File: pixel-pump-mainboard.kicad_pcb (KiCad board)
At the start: 4 copper layers, 68 x 67.3 mm, 123 parts, among them J1 JST NC Valve, J10 BM10B-SRSS-TB(LF)(SN), J11 UART/SWD DNP, J12 TYPE-C-31-M-12, J2 JST NO Valve, J3 6P4C, J4 JST 3 Way Valve, J5 Jack-DC, J6 Phoenix Contact 1733570, J7 BM04B-SRSS-TBT(LF)(SN), J8 SPI, J9 BM04B-SRSS-TBT(LF)(SN), Q1 BSS138, Q2 BSS138, Q3 BSS138, Q4 STN4NF20L, Q5 BSS138, SW1 BOOTSEL, U1 LD1117S33TR, U2 TPS62112RSAR, U3 W25Q128JVPIQ TR, U4 RP2040, Y1 ABMM2-12.000MHZ-E2-T

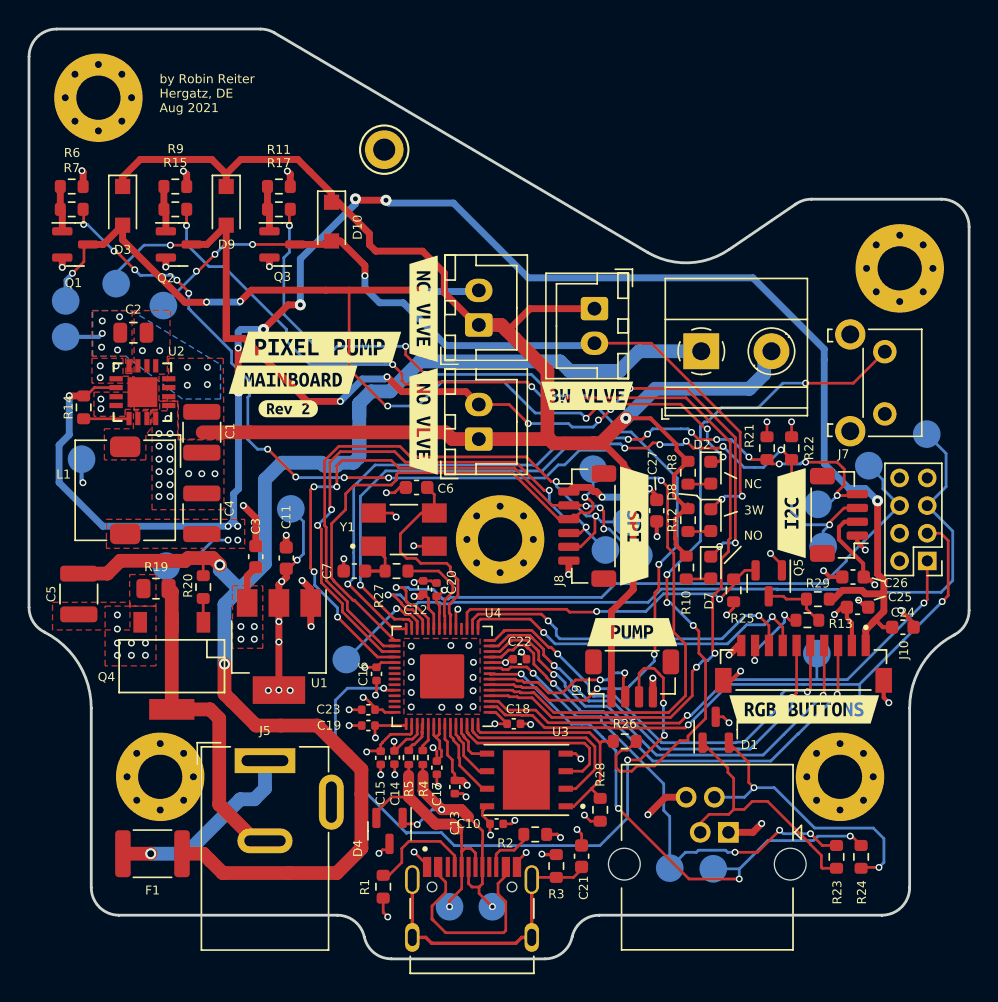
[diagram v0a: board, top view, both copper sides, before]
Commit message: Rename entire project to pixel pump
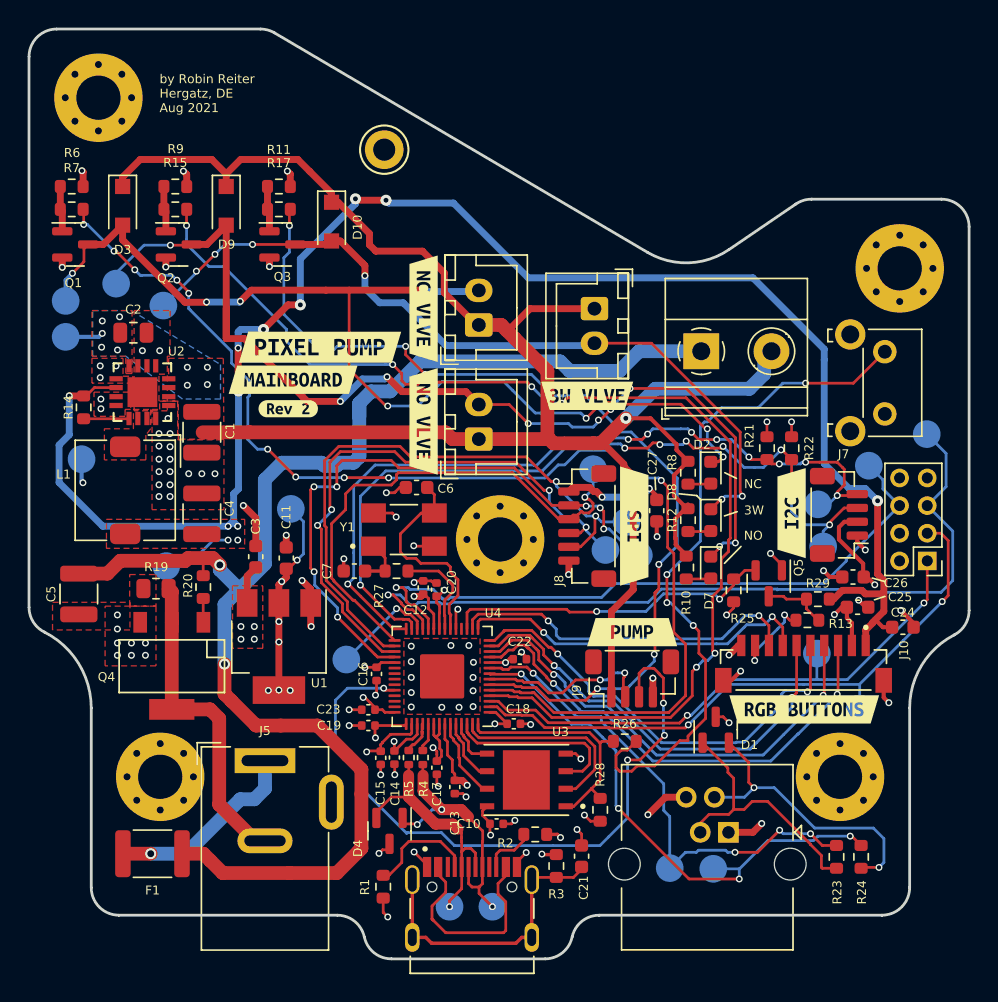
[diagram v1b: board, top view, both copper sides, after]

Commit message: Updated layout for EMI specific changes
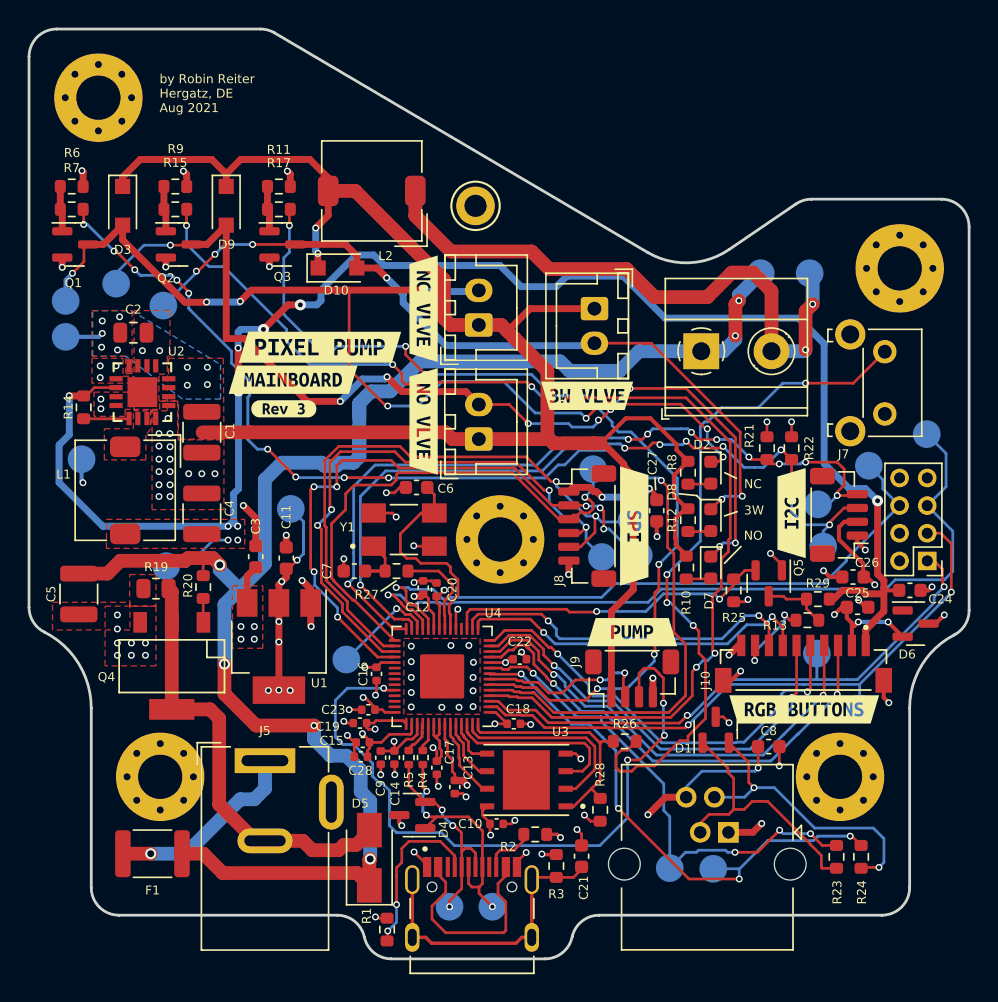
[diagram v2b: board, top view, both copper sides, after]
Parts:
- removed kibuzzard-61080B37: G***, kibuzzard-61080B37
- added C28: DNP, Capacitor_SMD:C_0402_1005Metric, F.Cu at (90.0, 143.0)
- added C8: 100n, Capacitor_SMD:C_0603_1608Metric, F.Cu at (119.5, 142.2)
- added C9: DNP, Capacitor_SMD:C_0402_1005Metric, F.Cu at (91.4, 143.0)
- added D5: SMAJ12CA, Diode_SMD:D_SMA, F.Cu at (90.6, 150.3)
- added D6: SP0502BAHT, Package_TO_SOT_SMD:SOT-23, F.Cu at (130.1, 133.3)
- added L2: 6.8uH, Inductor_SMD:L_TDK_SLF7032, F.Cu at (90.8, 102.0)
- added TP3: PSW1, TestPoint:TestPoint_Pad_D2.0mm, B.Cu at (118.9, 108.0)
- added TP6: PSW2, TestPoint:TestPoint_Pad_D2.0mm, B.Cu at (122.5, 108.0)
- added kibuzzard-61DF0B83: G***, kibuzzard-61DF0B83, F.Cu at (84.4, 117.8)
- C14, C15: value 1u -> 2.2u
- D2, D7, D8: value LED -> LED DNP
- J5: value Jack-DC -> Jack-DC 12V
- J6: value Phoenix Contact 1733570 -> Power Sw
- J7: value BM04B-SRSS-TBT(LF)(SN) -> I2C
- R10, R12, R8: value 68k -> 68k DNP
- R15, R17, R7: value 160 -> 220
- U3: value W25Q128JVPIQ TR -> W25Q128JVS
- moved TP19 7.75 mm to (98.3, 103.1)
- moved D10 3.38 mm to (88.3, 107.6), turned to 0 degrees
- moved R1 3.11 mm to (91.9, 155.5), turned to -90 degrees
- moved C24 2.71 mm to (129.7, 130.9)
- moved D4 2.01 mm to (93.7, 147.2), turned to 180 degrees
- moved C15 1.71 mm to (90.1, 141.9), turned to 180 degrees
- moved C19 0.64 mm to (89.9, 140.5)
- moved TP27 0.57 mm to (107.4, 128.5)
- moved TP28 0.40 mm to (109.6, 125.9)
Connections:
- J6 pad 2: +12V -> Net-(J6-Pad2)
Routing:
- net Net-(J6-Pad2): track 0.00 -> 44.0 mm, vias 0 -> 2
- net +3V3: track 71.9 -> 85.6 mm, vias 26 -> 29
- net Net-(C5-Pad1): track 105.2 -> 117.2 mm, vias 2 -> 6
- net Net-(D5-Pad2): track 23.2 -> 31.7 mm
- net +12V: track 137.2 -> 129.8 mm, vias 10 -> 11
- net +5V: track 130.0 -> 125.4 mm, vias 16 -> 14
- net Net-(J12-PadA5): track 8.27 -> 12.4 mm, vias 0 -> 2
- net DN: track 18.8 -> 14.9 mm, vias 1 -> 3
- net GND: track 59.7 -> 62.8 mm, vias 91 -> 94
- net UART0_RX: track 40.7 -> 42.4 mm
- net Net-(D7-Pad1): track 73.4 -> 72.0 mm
- net BEMF: track 49.4 -> 50.3 mm
- net DP: track 18.6 -> 17.8 mm
- net Drop Btn: track 34.6 -> 33.8 mm
- net +1V1: track 31.5 -> 32.3 mm
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
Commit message: Finish EMI changes
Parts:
- moved D5 0.37 mm to (90.5, 150.6), turned to -90 degrees
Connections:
- D5 pad 1: Net-(C5-Pad1) -> Net-(J5-Pad1)
- F1 pad 2: Net-(F1-Pad2) -> Net-(J5-Pad1)
- J5 pad 1: Net-(F1-Pad2) -> Net-(J5-Pad1)
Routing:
- net Net-(J5-Pad1): track 0.00 -> 37.6 mm, vias 0 -> 2
- net Net-(C5-Pad1): track 117.2 -> 95.2 mm
- net Net-(F1-Pad2): track 14.2 -> 0.00 mm, vias 1 -> 0
- net +1V1: track 32.3 -> 32.9 mm
- net Net-(D5-Pad2): track 31.7 -> 32.2 mm
- net BEMF: track 50.3 -> 50.7 mm, vias 4 -> 6

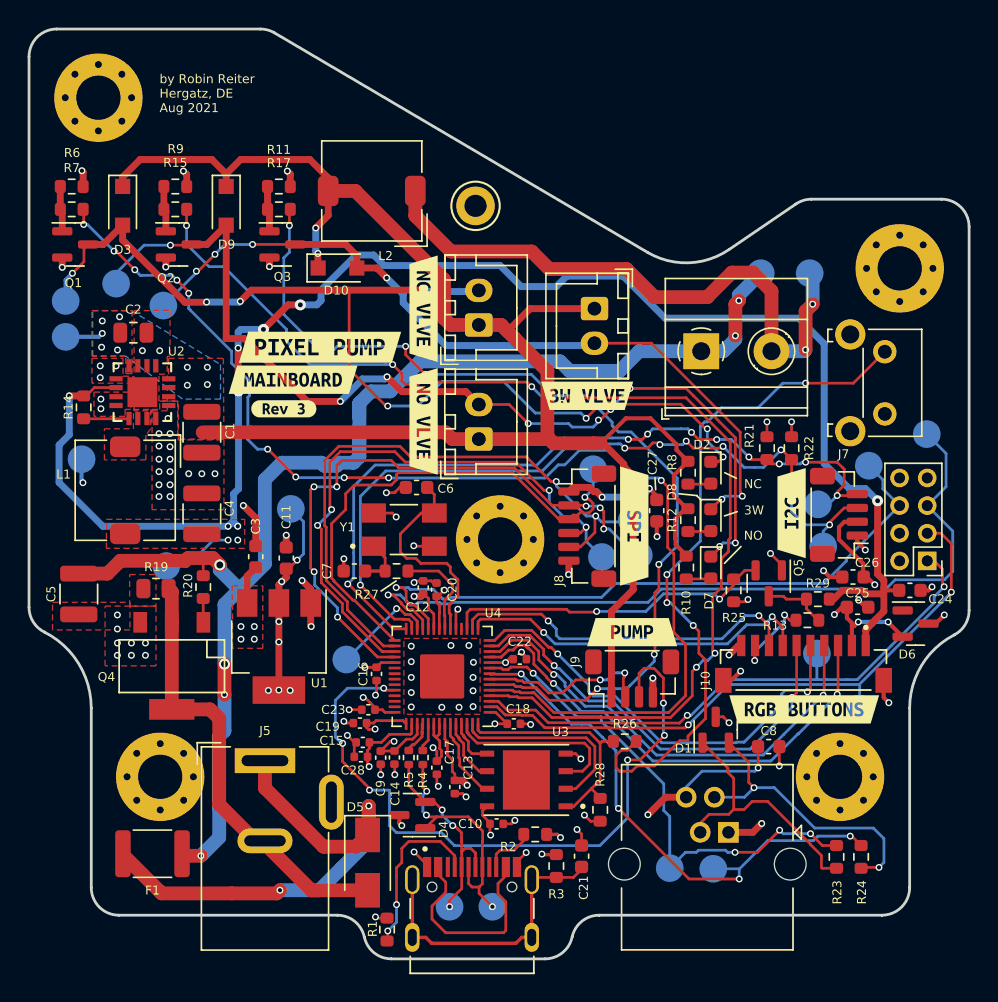
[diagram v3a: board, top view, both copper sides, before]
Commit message: Adjusted spacing between testpoints
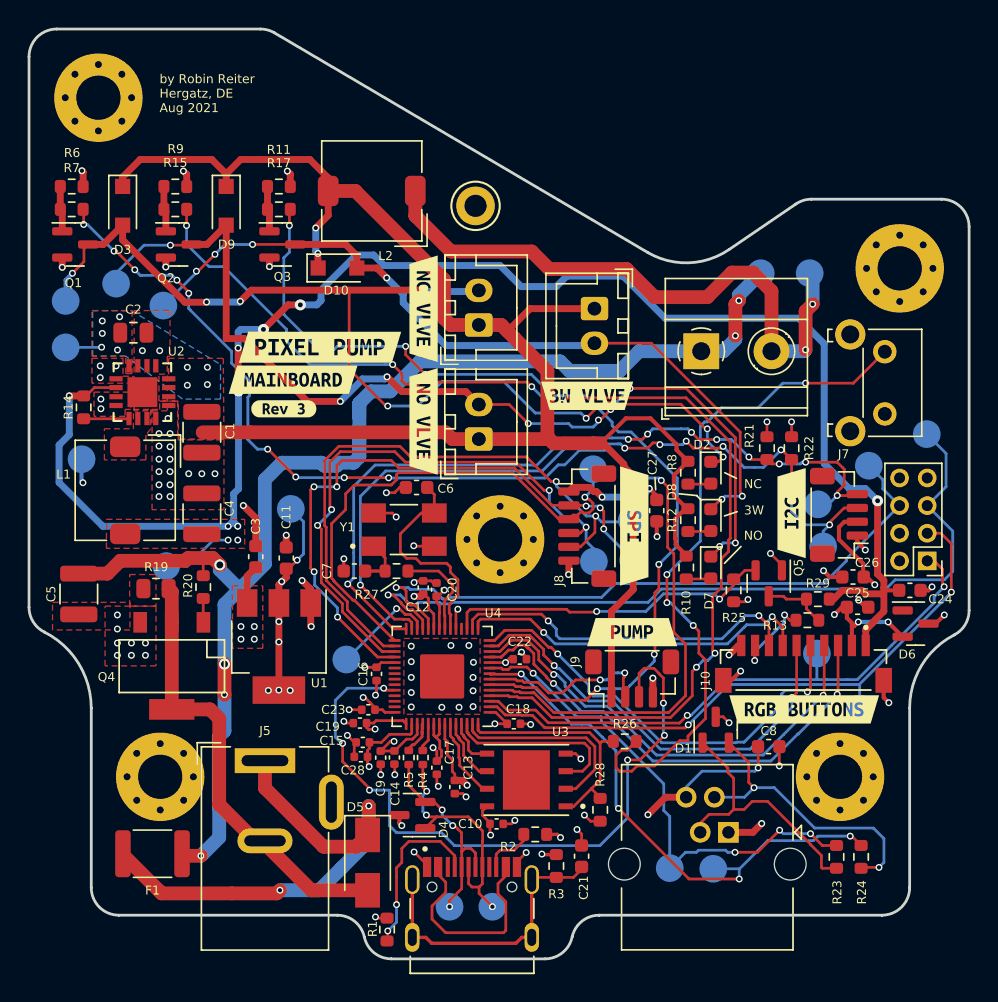
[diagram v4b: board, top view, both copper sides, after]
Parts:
- moved TP10 0.76 mm to (68.7, 113.4)
- moved TP27 0.67 mm to (106.9, 128.9)
- moved TP25 0.54 mm to (109.7, 128.8)
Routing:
- net Net-(D5-Pad1): track 37.6 -> 36.8 mm
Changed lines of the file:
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@@
   (net 15 "Net-(C5-Pad1)")
   (net 16 "FOOTPEDAL_AUX")
-  (net 17 "Net-(J5-Pad1)")
+  (net 17 "Net-(D5-Pad1)")
   (net 18 "Net-(C21-Pad2)")
   (net 19 "I2C0_SDA")
@@
     (fp_line (start -0.64944 0.00102) (end 0.50118 -0.79908) (layer "F.Fab") (width 0.1))
     (pad "1" smd rect locked (at -2 0 270) (size 2.5 1.8) (layers "F.Cu" "F.Paste" "F.Mask")
-      (net 17 "Net-(J5-Pad1)") (pinfunction "1") (pintype "passive"))
+      (net 17 "Net-(D5-Pad1)") (pinfunction "1") (pintype "passive"))
     (pad "2" smd rect locked (at 2 0 270) (size 2.5 1.8) (layers "F.Cu" "F.Paste" "F.Mask")
       (net 46 "Net-(D5-Pad2)") (pinfunction "2") (pintype "passive"))
@@
     (fp_line (start 4.5 13.6) (end -4.5 13.6) (layer "F.Fab") (width 0.1))
     (pad "1" thru_hole rect locked (at 0 0) (size 4.4 1.8) (drill oval 3.4 0.8) (layers *.Cu *.Mask)
-      (net 17 "Net-(J5-Pad1)") (pintype "passive"))
+      (net 17 "Net-(D5-Pad1)") (pintype "passive"))
     (pad "2" thru_hole oval locked (at 0 5.8) (size 4 1.8) (drill oval 3 0.8) (layers *.Cu *.Mask)
       (net 46 "Net-(D5-Pad2)") (pintype "passive"))
@@
       (net 15 "Net-(C5-Pad1)") (pintype "passive"))
     (pad "2" smd roundrect locked (at 2.1375 0 180) (size 1.125 3.4) (layers "F.Cu" "F.Paste" "F.Mask") (roundrect_rratio 0.2222222222)
-      (net 17 "Net-(J5-Pad1)") (pintype "passive"))
+      (net 17 "Net-(D5-Pad1)") (pintype "passive"))
     (model "${KICAD6_3DMODEL_DIR}/Fuse.3dshapes/Fuse_1812_4532Metric.wrl"
       (offset (xyz 0 0 0))
@@
   )
   (footprint "TestPoint:TestPoint_Pad_D2.0mm" (layer "B.Cu")
-    (at 68.65 112.6 180)
+    (at 68.65 113.362 180)
     (descr "SMD pad as test Point, diameter 2.0mm")
     (tags "test point SMD pad")
@@
   )
   (footprint "TestPoint:TestPoint_Pad_D2.0mm" (layer "B.Cu")
-    (at 110.109 128.397 180)
+    (at 109.7026 128.7526 180)
     (descr "SMD pad as test Point, diameter 2.0mm")
     (tags "test point SMD pad")
@@
   )
   (footprint "TestPoint:TestPoint_Pad_D2.0mm" (layer "B.Cu")
-    (at 107.442 128.524 180)
+    (at 106.8578 128.8542 180)
     (descr "SMD pad as test Point, diameter 2.0mm")
     (tags "test point SMD pad")
@@
   (segment (start 92.4224 142.5582) (end 92.4306 142.55) (width 0.2) (layer "F.Cu") (net 5))
   (segment (start 93.853 131.3688) (end 94.3558 131.3688) (width 0.5) (layer "F.Cu") (net 5))
-  (segment (start 92.4306 141.8844) (end 92.4052 141.859) (width 0.2) (layer "F.Cu") (net 5))
   (segment (start 92.1376 141.859) (end 91.4384 142.5582) (width 0.2) (layer "F.Cu") (net 5))
   (segment (start 95.28 132.6434) (end 95.28 133.7225) (width 0.2) (layer "F.Cu") (net 5))
@@
   (segment (start 83.9216 152.8572) (end 84.1502 152.6286) (width 1) (layer "F.Cu") (net 17))
   (segment (start 80.6704 152.8572) (end 83.9216 152.8572) (width 1) (layer "F.Cu") (net 17))
-  (segment (start 90.487 148.6328) (end 89.6954 148.6328) (width 0.2) (layer "F.Cu") (net 17))
   (segment (start 75.5904 152.8572) (end 80.6704 152.8572) (width 1) (layer "F.Cu") (net 17))
   (segment (start 89.6408 149.479) (end 90.487 148.6328) (width 1) (layer "F.Cu") (net 17))
@@
   (via (at 86.6225 129.5908) (size 0.5) (drill 0.3) (layers "F.Cu" "B.Cu") (net 21))
   (via (at 88.3158 132.8674) (size 0.5) (drill 0.3) (layers "F.Cu" "B.Cu") (net 21))
-  (segment (start 109.865924 128.397) (end 107.960924 126.492) (width 0.2) (layer "B.Cu") (net 21))
-  (segment (start 107.960924 126.492) (end 107.569 126.492) (width 0.2) (layer "B.Cu") (net 21))
+  (segment (start 107.569 126.492) (end 107.569 126.619) (width 0.2) (layer "B.Cu") (net 21))
   (segment (start 88.3158 132.207) (end 86.6648 130.556) (width 0.2) (layer "B.Cu") (net 21))
   (segment (start 106.299 124.841) (end 107.188 124.841) (width 0.2) (layer "B.Cu") (net 21))
@@
   (segment (start 107.188 124.841) (end 107.315 124.968) (width 0.2) (layer "B.Cu") (net 21))
   (segment (start 88.3158 132.8674) (end 88.3158 132.207) (width 0.2) (layer "B.Cu") (net 21))
+  (segment (start 107.569 126.619) (end 109.7026 128.7526) (width 0.2) (layer "B.Cu") (net 21))
   (segment (start 100.965 122.428) (end 104.3258 125.7888) (width 0.2) (layer "F.Cu") (net 22))
   (segment (start 92.202 123.317) (end 92.583 122.936) (width 0.2) (layer "F.Cu") (net 22))
@@
   (segment (start 105.664 125.73) (end 104.775 125.73) (width 0.2) (layer "B.Cu") (net 23))
   (segment (start 106.299 126.365) (end 105.664 125.73) (width 0.2) (layer "B.Cu") (net 23))
+  (segment (start 106.8578 127.9398) (end 106.8578 128.8542) (width 0.2) (layer "B.Cu") (net 23))
   (segment (start 106.299 127.381) (end 106.299 126.365) (width 0.2) (layer "B.Cu") (net 23))
-  (segment (start 107.442 128.524) (end 106.299 127.381) (width 0.2) (layer "B.Cu") (net 23))
+  (segment (start 106.299 127.381) (end 106.8578 127.9398) (width 0.2) (layer "B.Cu") (net 23))
   (segment (start 87.884 125.222) (end 86.868 126.238) (width 0.2) (layer "B.Cu") (net 23))
   (segment (start 104.775 125.73) (end 103.632 124.587) (width 0.2) (layer "B.Cu") (net 23))
@@
   (via (at 71.3 111.45) (size 0.5) (drill 0.3) (layers "F.Cu" "B.Cu") (free) (net 77))
   (via (at 71.25 113.35) (size 0.5) (drill 0.3) (layers "F.Cu" "B.Cu") (free) (net 77))
+  (segment (start 71.238 113.362) (end 71.25 113.35) (width 0.2) (layer "B.Cu") (net 77))
+  (segment (start 68.65 113.362) (end 71.238 113.362) (width 0.2) (layer "B.Cu") (net 77))
   (segment (start 86.741 104.7242) (end 86.741 106.4121) (width 0.5) (layer "B.Cu") (net 77))
-  (segment (start 68.65 112.6) (end 71.05 112.6) (width 0.3) (layer "B.Cu") (net 77))
   (segment (start 86.741 106.4121) (end 86.8934 106.5645) (width 0.5) (layer "B.Cu") (net 77))
-  (segment (start 71.05 112.6) (end 71.3 112.35) (width 0.3) (layer "B.Cu") (net 77))
   (segment (start 126.492 131.191) (end 127.762 131.191) (width 0.5) (layer "F.Cu") (net 78))
   (segment (start 70.7302 116.2698) (end 72.295 116.2698) (width 0.2) (layer "F.Cu") (net 78))
@@
   (segment (start 124.7902 132.1562) (end 124.2568 132.6896) (width 0.3) (layer "F.Cu") (net 80))
   (segment (start 98.806 146.883) (end 99.131 146.558) (width 0.2) (layer "F.Cu") (net 80))
-  (segment (start 90.6246 141.9352) (end 90.6246 141.8056) (width 0.2) (layer "F.Cu") (net 80))
   (segment (start 84.6074 129.3752) (end 84.6074 129.9972) (width 0.5) (layer "F.Cu") (net 80))
   (segment (start 91.1352 136.5022) (end 90.3198 136.5022) (width 0.2) (layer "F.Cu") (net 80))
